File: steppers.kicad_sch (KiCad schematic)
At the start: 9 parts, among them J4 Screw_Terminal_01x02

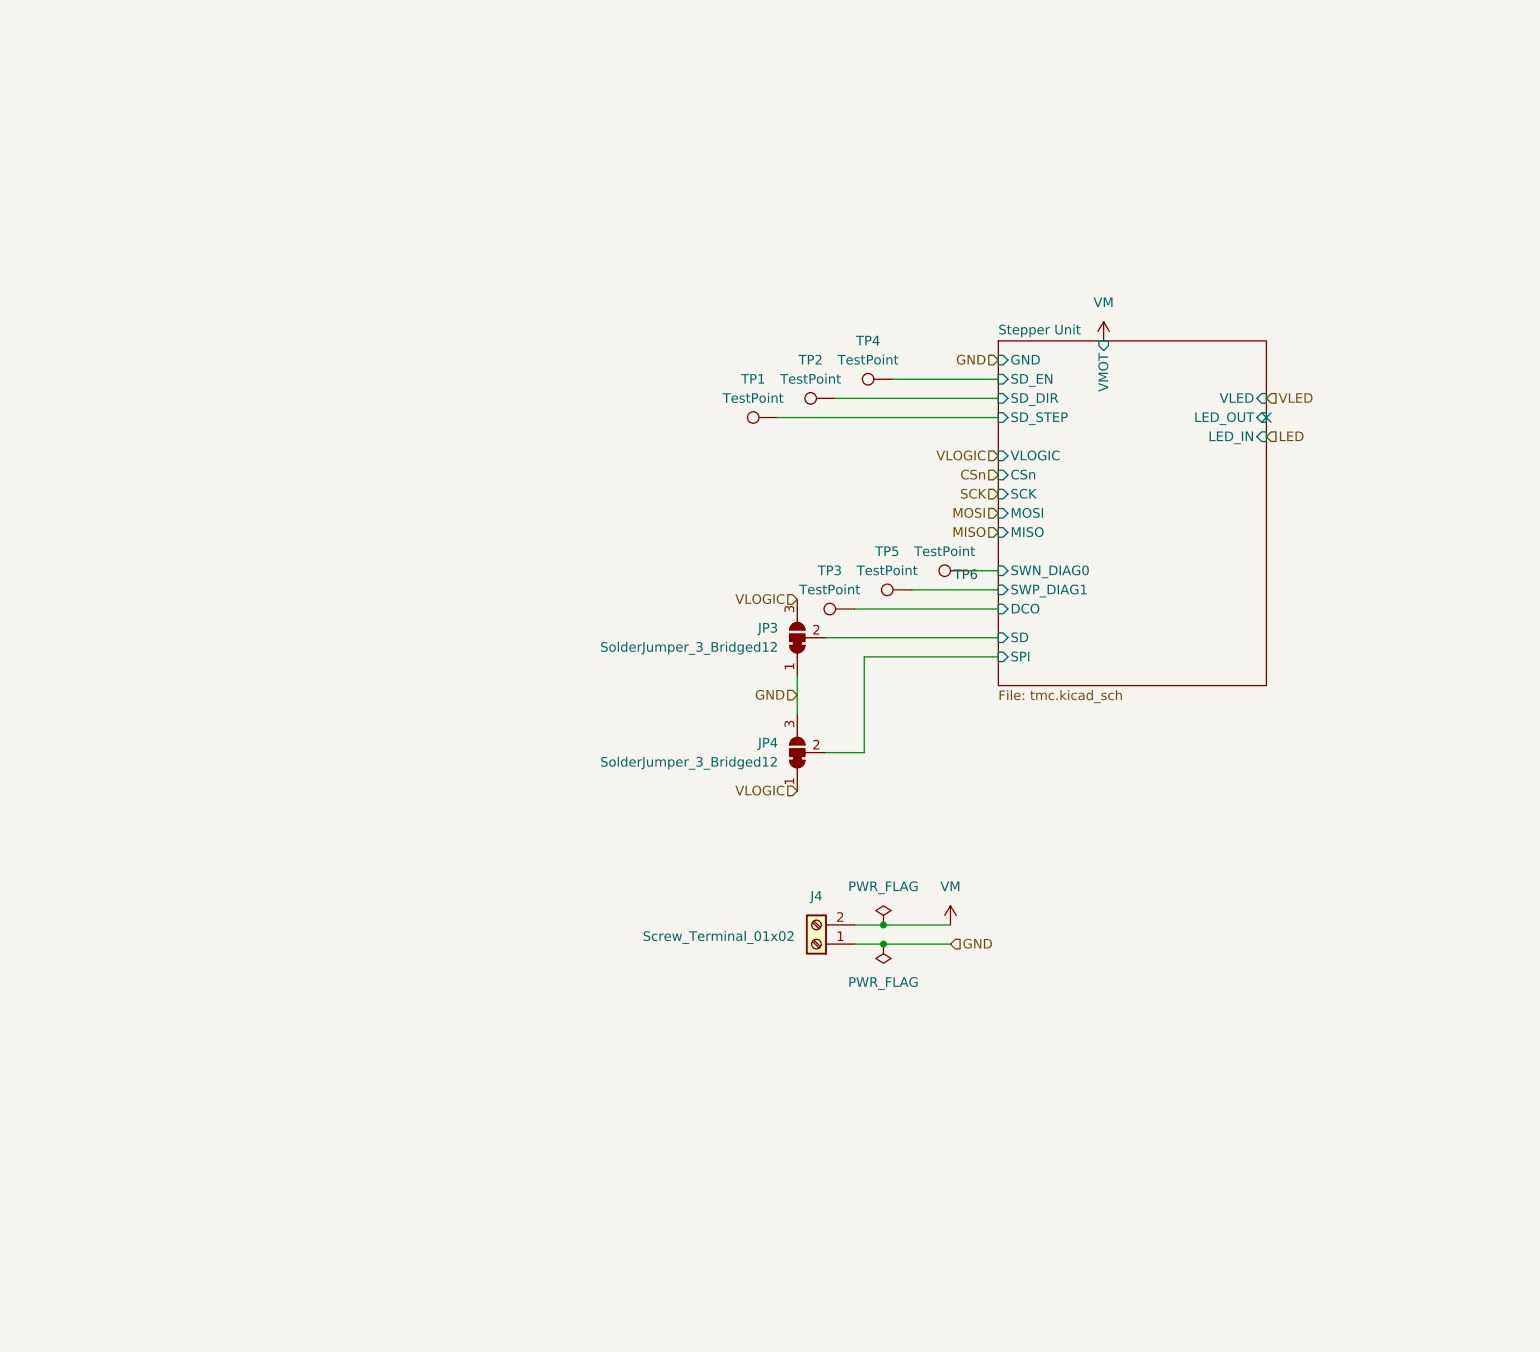
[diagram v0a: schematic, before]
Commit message: x4 stepper units
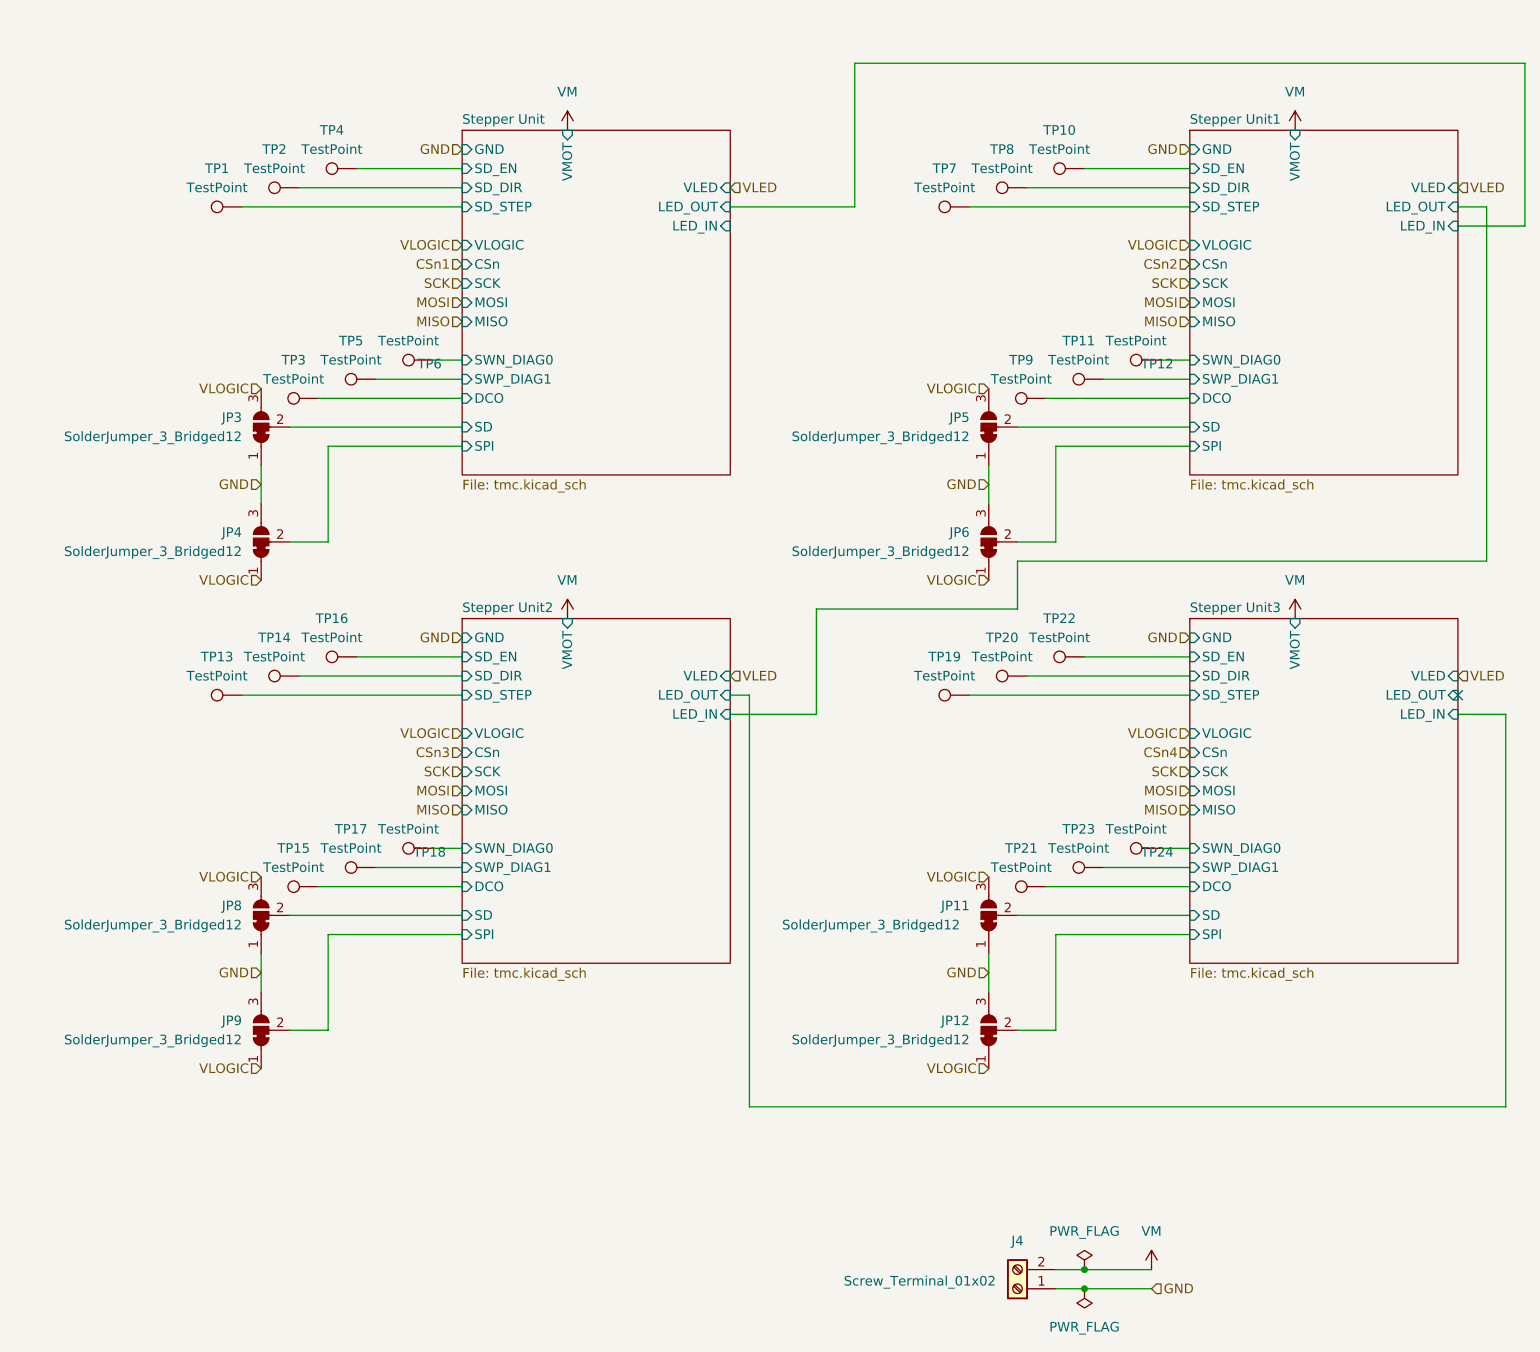
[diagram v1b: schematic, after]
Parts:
- added JP11, JP12, JP5, JP6, JP8, JP9: SolderJumper_3_Bridged12, Jumper:SolderJumper-3_P1.3mm_Bridged12_RoundedPad1.0x1.5mm, symbol Jumper:SolderJumper_3_Bridged12
- added TP10, TP11, TP12, TP13, TP14, TP15, TP16, TP17, TP18, TP19, TP20, TP21, TP22, TP23, TP24, TP7, TP8, TP9: TestPoint, TestPoint:TestPoint_Pad_D1.5mm, symbol Connector:TestPoint
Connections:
- net GND: now also JP11.1 (A), JP12.3 (B), JP5.1 (A), JP6.3 (B), JP8.1 (A), JP9.3 (B)
- net VLOGIC: now also JP11.3 (B), JP12.1 (A), JP5.3 (B), JP6.1 (A), JP8.3 (B), JP9.1 (A)
- new net Stepper Unit1/DCO: TP9.1
- new net Stepper Unit1/SD: JP5.2 (C)
- new net Stepper Unit1/SD_DIR: TP8.1
- new net Stepper Unit1/SD_EN: TP10.1
- new net Stepper Unit1/SD_STEP: TP7.1
- new net Stepper Unit1/SPI: JP6.2 (C)
- new net Stepper Unit1/SWN_DIAG0: TP12.1
- new net Stepper Unit1/SWP_DIAG1: TP11.1
- new net Stepper Unit2/DCO: TP15.1
- new net Stepper Unit2/SD: JP8.2 (C)
- new net Stepper Unit2/SD_DIR: TP14.1
- new net Stepper Unit2/SD_EN: TP16.1
- new net Stepper Unit2/SD_STEP: TP13.1
- new net Stepper Unit2/SPI: JP9.2 (C)
- new net Stepper Unit2/SWN_DIAG0: TP18.1
- new net Stepper Unit2/SWP_DIAG1: TP17.1
- new net Stepper Unit3/DCO: TP21.1
- new net Stepper Unit3/SD: JP11.2 (C)
- new net Stepper Unit3/SD_DIR: TP20.1
- new net Stepper Unit3/SD_EN: TP22.1
- new net Stepper Unit3/SD_STEP: TP19.1
- new net Stepper Unit3/SPI: JP12.2 (C)
- new net Stepper Unit3/SWN_DIAG0: TP24.1
- new net Stepper Unit3/SWP_DIAG1: TP23.1
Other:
- added sheet Stepper Unit1 (tmc.kicad_sch)
- added sheet Stepper Unit2 (tmc.kicad_sch)
- added sheet Stepper Unit3 (tmc.kicad_sch)
- moved on the sheet: J4, JP3, JP4, TP1, TP2, TP3, TP4, TP5, TP6

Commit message: Lots of work
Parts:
- removed JP11, JP12, JP3, JP4, JP5, JP6, JP8, JP9: SolderJumper_3_Bridged12, Jumper:SolderJumper-3_P1.3mm_Bridged12_RoundedPad1.0x1.5mm, symbol Jumper:SolderJumper_3_Bridged12
- removed TP1, TP10, TP13, TP14, TP16, TP19, TP2, TP20, TP22, TP4, TP7, TP8: TestPoint, TestPoint:TestPoint_Pad_D1.5mm, symbol Connector:TestPoint
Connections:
- no-connect marks 1 -> 13

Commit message: first stepper unit
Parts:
- removed J4: Screw_Terminal_01x02, Connector_Phoenix_SPT:PhoenixContact_SPT_5_2-H-7.5-ZB_1x02_P7.5mm_Horizontal, symbol Connector:Screw_Terminal_01x02
- removed TP11, TP12, TP15, TP17, TP18, TP21, TP23, TP24, TP3, TP5, TP6, TP9: TestPoint, TestPoint:TestPoint_Pad_D1.5mm, symbol Connector:TestPoint
- added J10, J11, J8, J9: Screw_Terminal_01x02, Connector_Phoenix_MSTB:PhoenixContact_MSTBVA_2,5_2-G-5,08_1x02_P5.08mm_Vertical, symbol Connector:Screw_Terminal_01x02
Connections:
- net GND: now also J10.1 (Pin_1), J11.1 (Pin_1), J8.1 (Pin_1), J9.1 (Pin_1)
- new net Stepper Unit/VMOT: J8.2 (Pin_2)
- new net Stepper Unit1/VMOT: J9.2 (Pin_2)
- new net Stepper Unit2/VMOT: J11.2 (Pin_2)
- new net Stepper Unit3/VMOT: J10.2 (Pin_2)
- no-connect marks 13 -> 25

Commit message: Updated footprints, digikey parts
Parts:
- J10, J11, J8, J9: Part (none) -> 1755736
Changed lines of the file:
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@@
+			)
+		)
+		(property "Part" "1755736"
+			(at 146.05 88.9 0)
+			(effects
+				(font
+					(size 1.27 1.27)
+				)
+				(hide yes)
 			)
 		)
@@
 			)
 		)
+		(property "Part" "1755736"
+			(at 49.53 24.13 0)
+			(effects
+				(font
+					(size 1.27 1.27)
+				)
+				(hide yes)
+			)
+		)
 		(pin "1"
 		)
@@
 			)
 		)
+		(property "Part" "1755736"
+			(at 146.05 24.13 0)
+			(effects
+				(font
+					(size 1.27 1.27)
+				)
+				(hide yes)
+			)
+		)
 		(pin "1"
 		)
@@
 			(at 49.53 88.9 0)
 			(effects
+				(font
+					(size 1.27 1.27)
+				)
+				(hide yes)
+			)
+		)
+		(property "Part" "1755736"
+			(at 49.53 88.9 0)
+			(effects
